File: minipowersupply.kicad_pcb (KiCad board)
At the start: 2 copper layers, 91 x 60.4 mm, 112 parts, among them J1 Conn_01x01_Female, J10 Conn_01x08_Male, J2 Conn_01x01_Female, J3 Conn_01x01_Female, J4 Conn_01x01_Female, J5 Conn_01x01_Female, J6 Conn_01x01_Female, J7 Conn_01x01_Female, J8 Conn_01x02_Female, J9 Conn_01x02_Female, Q1 BC817, U1 LM317_TO-220, U10 74HC4051, U11 74HC4051, U12 LM358, U13 LM358, U2 LM337_TO220, U3 LM7805_TO220, U4 ACS70331EOLCTR-2P5U3, U5 ACS70331EOLCTR-2P5U3, U6 ACS70331EOLCTR-2P5U3, U7 ACS70331EOLCTR-2P5U3, U8 ACS70331EOLCTR-2P5U3, U9 LM358

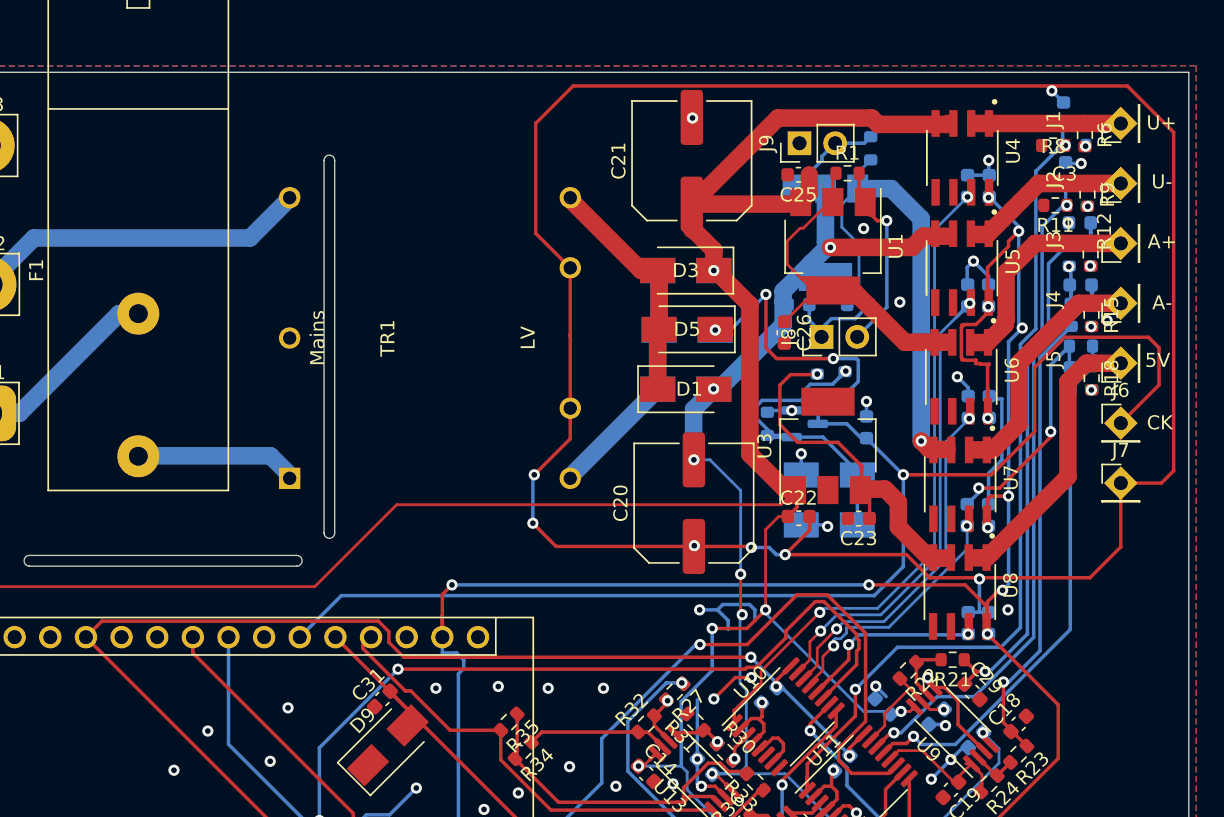
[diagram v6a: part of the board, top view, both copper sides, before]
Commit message: improved earthing and created ring track to isolate supply from display electronics
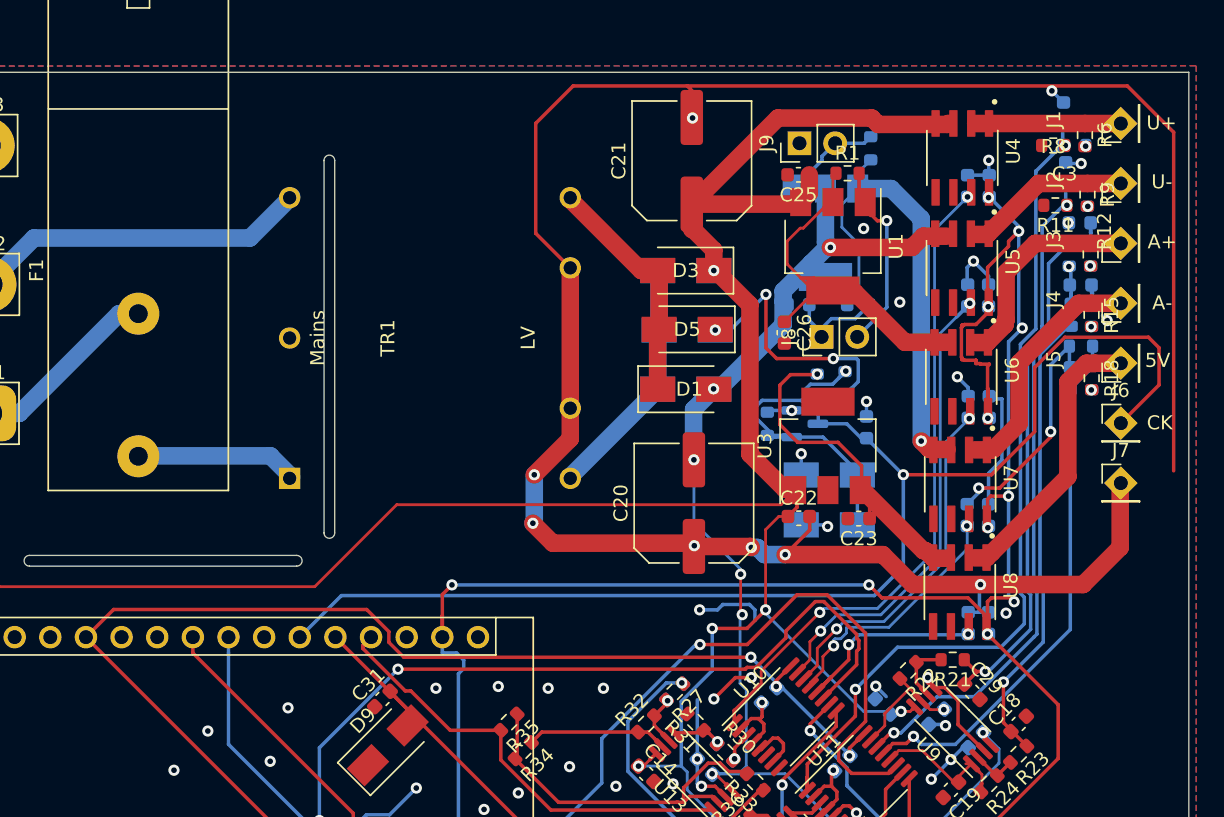
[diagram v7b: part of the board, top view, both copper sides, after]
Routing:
- net GNDREF: track 287.0 -> 290.3 mm
- net 3V3: track 164.8 -> 165.8 mm
- net /Clock and TTL/V5Out: track 26.8 -> 25.8 mm
- net V5: track 89.7 -> 90.4 mm
- net VUnreg-: track 95.7 -> 95.1 mm

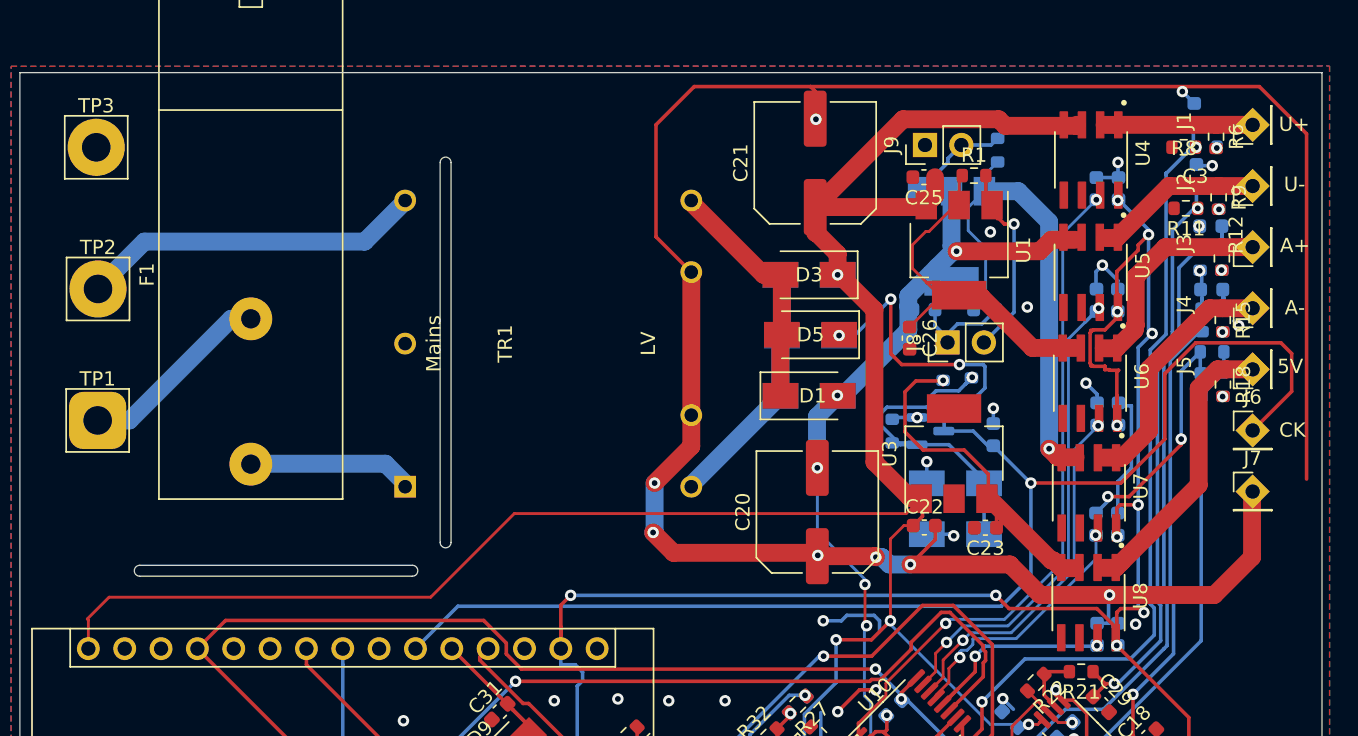
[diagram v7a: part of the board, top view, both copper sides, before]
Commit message: small position adjustments to attain required spacing
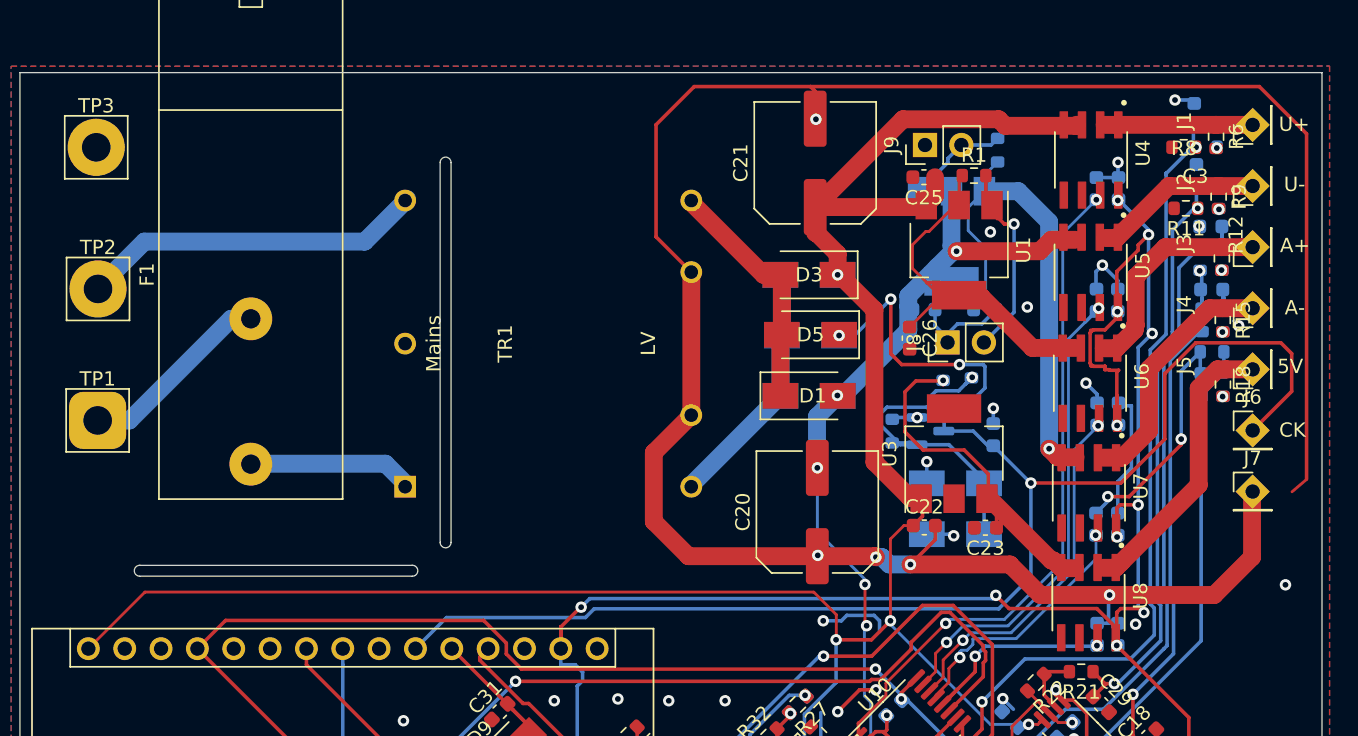
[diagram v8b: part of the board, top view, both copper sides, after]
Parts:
- moved R10 0.05 mm to (171.1, 78.6)
- moved R9 0.05 mm to (171.1, 78.6)
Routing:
- net VUnreg+: track 177.6 -> 170.0 mm
- net GNDREF: track 290.3 -> 289.1 mm, vias 57 -> 55
- net 3V3: track 165.8 -> 164.9 mm
